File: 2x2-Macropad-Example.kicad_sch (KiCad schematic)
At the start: 24 parts, among them SW1 SW_Push, U1 ATmega32U4-A, Y1 16MHz

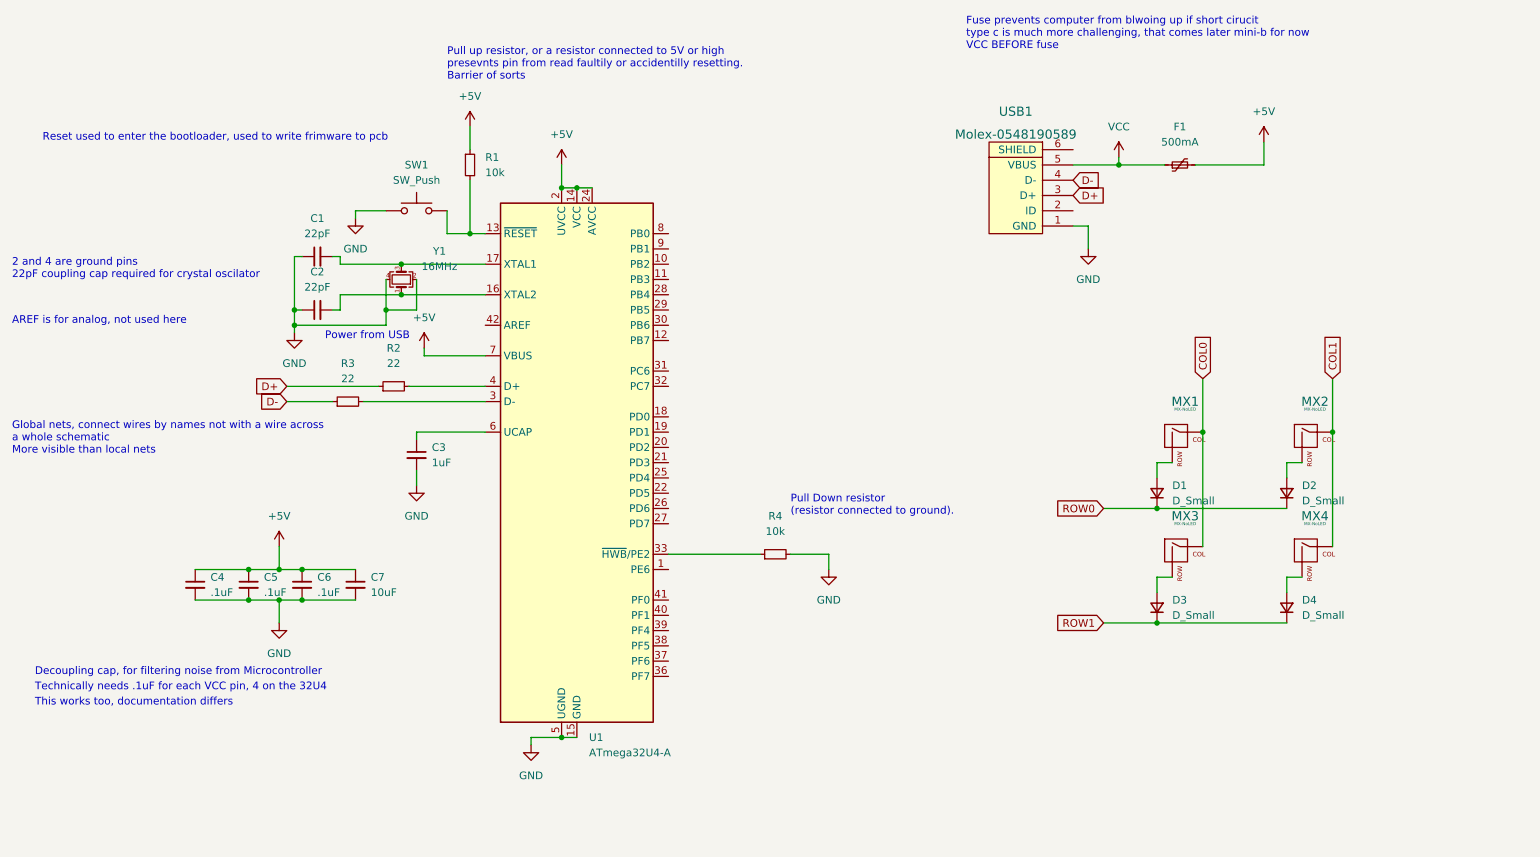
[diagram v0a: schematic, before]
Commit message: finished routing and laying fills, DRC issue with usb and mx footprints
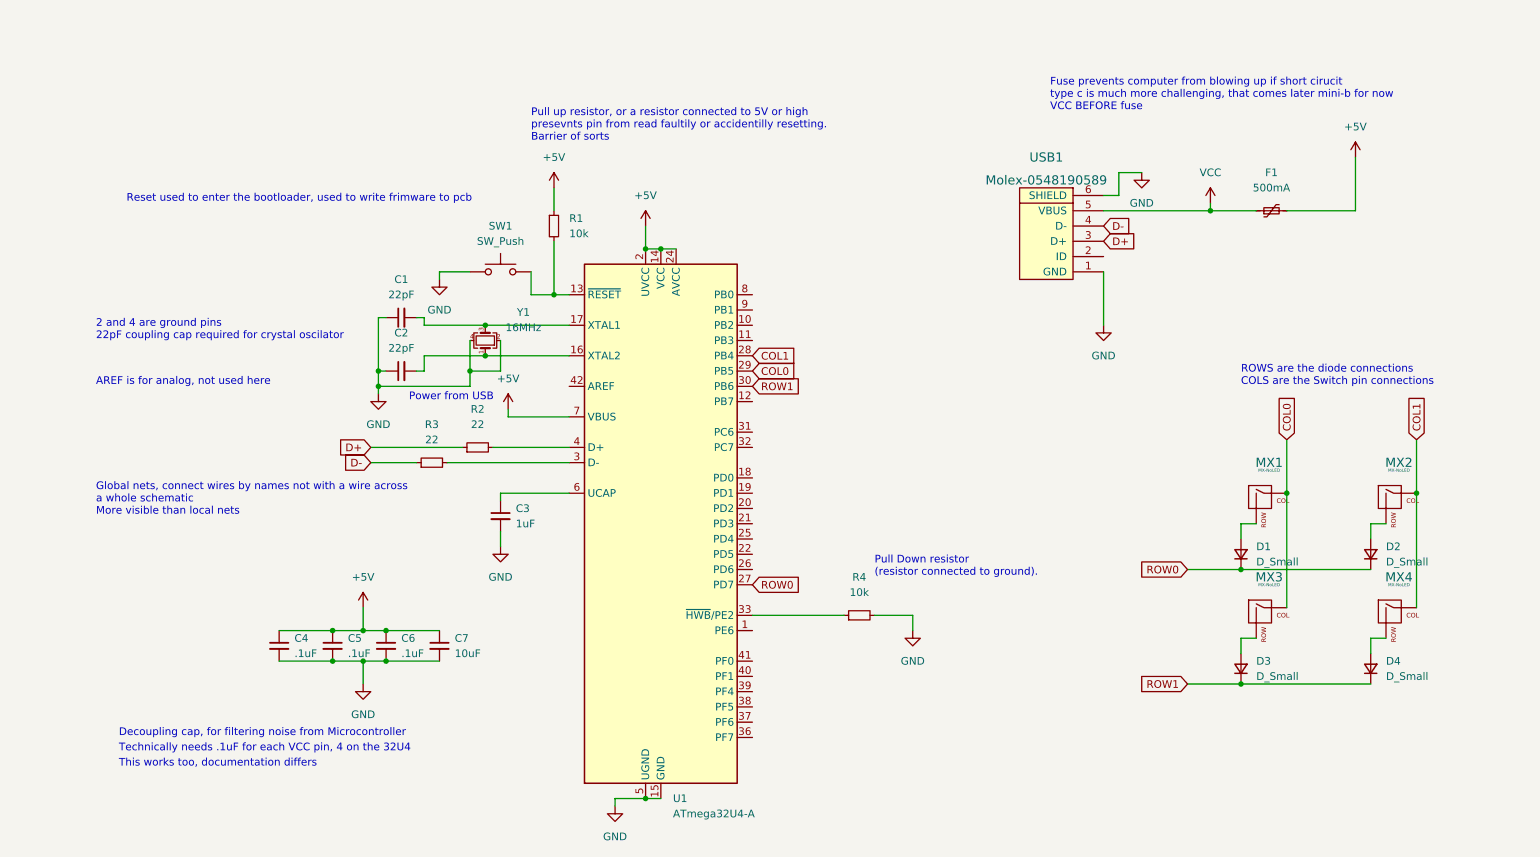
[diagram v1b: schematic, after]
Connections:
- net COL0: now also U1.29 (PB5)
- net COL1: now also U1.28 (PB4)
- net GND: now also USB1.6 (SHIELD)
- net ROW0: now also U1.27 (PD7)
- net ROW1: now also U1.30 (PB6)
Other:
- note added: "Fuse prevents computer from blowing up if short cirucit type c is much more challenging, that comes later mini-b for now VCC BEFORE fuse"
- note added: "ROWS are the diode connections COLS are the Switch pin connections"
- note removed: "Fuse prevents computer from blwoing up if short cirucit type c is much more challenging, that comes later mini-b for now VCC BEFORE fuse"
- moved on the sheet: C1, C2, C3, C4, C5, C6, C7, D1, D2, D3, D4, F1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
